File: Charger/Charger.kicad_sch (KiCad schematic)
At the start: 9 parts, among them J1 Bat_ballanser_conn, J2 Battery_conn, J3 Power_conn, J4 Screen_SPInCtrlnPwr_Conn, J5 User_Interface_Conn, J8 Temp_Sens_Conn

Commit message: PCB V1
do przerobienia jedynie numery elementów na wartości jedno i drugi w miare poukladane tylko podmienic i posprawdzać
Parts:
- J3: footprint Connector_AMASS:AMASS_XT60PW-F_1x02_P7.20mm_Horizontal -> Connector_AMASS:AMASS_XT60PW-M_1x02_P7.20mm_Horizontal
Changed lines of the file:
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@@
 			)
 		)
-		(property "Footprint" "Connector_AMASS:AMASS_XT60PW-F_1x02_P7.20mm_Horizontal"
+		(property "Footprint" "Connector_AMASS:AMASS_XT60PW-M_1x02_P7.20mm_Horizontal"
 			(at 25.4 52.07 0)
 			(effects

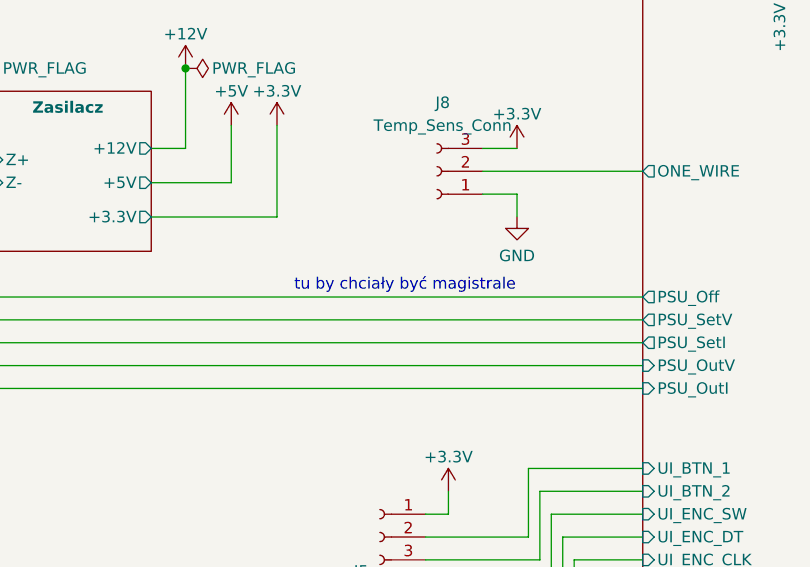
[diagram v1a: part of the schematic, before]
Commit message: Changed SPI connector and MUX pins
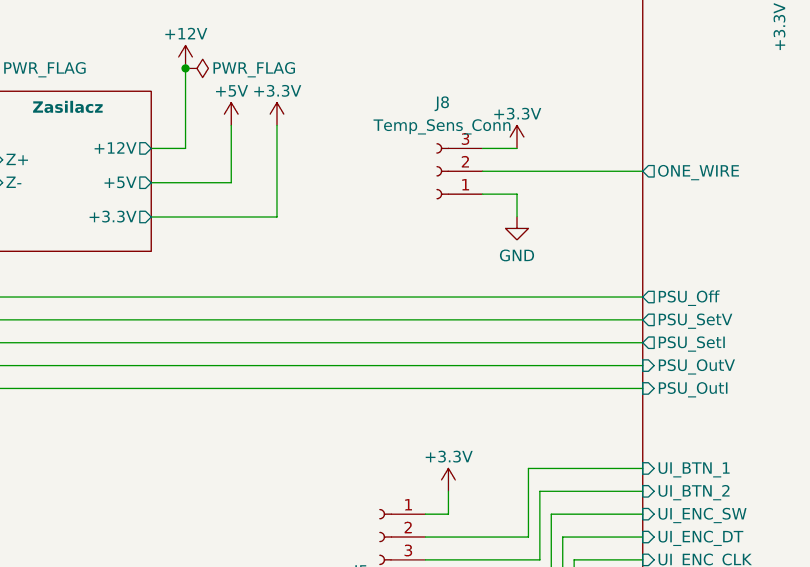
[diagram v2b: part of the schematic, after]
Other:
- note removed: "tu by chciały być magistrale"
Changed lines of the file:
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@@
-		)
-	)
-	(text "tu by chciały być magistrale"
-		(exclude_from_sim no)
-		(at 92.964 66.04 0)
-		(effects
-			(font
-				(size 1.27 1.27)
-			)
 		)
 	)

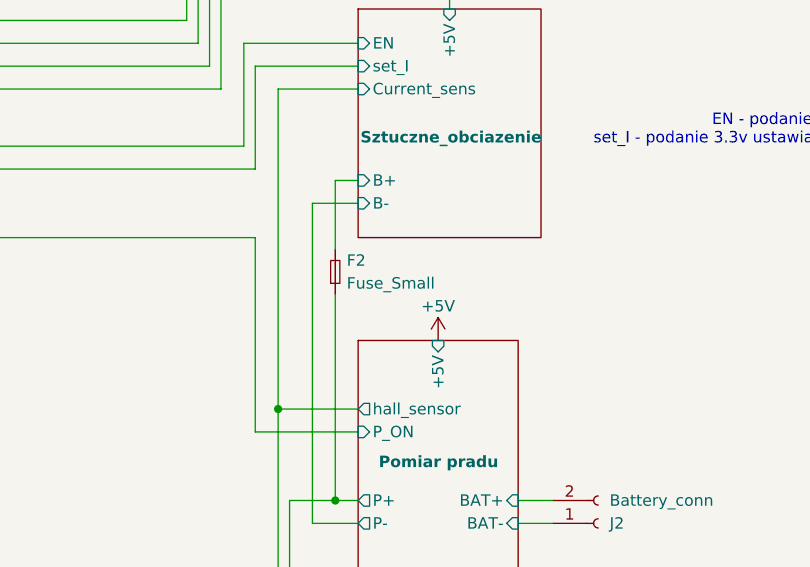
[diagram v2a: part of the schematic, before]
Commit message: up
zmienione kilka sciezek, dodane przelotki do masy i rezystor do adc
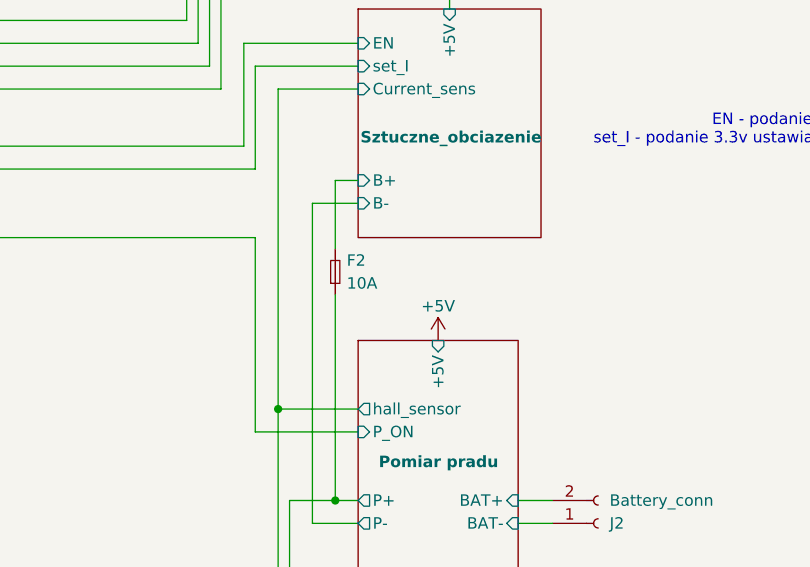
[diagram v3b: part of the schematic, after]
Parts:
- F2: value Fuse_Small -> 10A
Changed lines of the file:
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@@
 			)
 		)
-		(property "Value" "Fuse_Small"
+		(property "Value" "10A"
 			(at 213.36 107.9499 90)
 			(effects

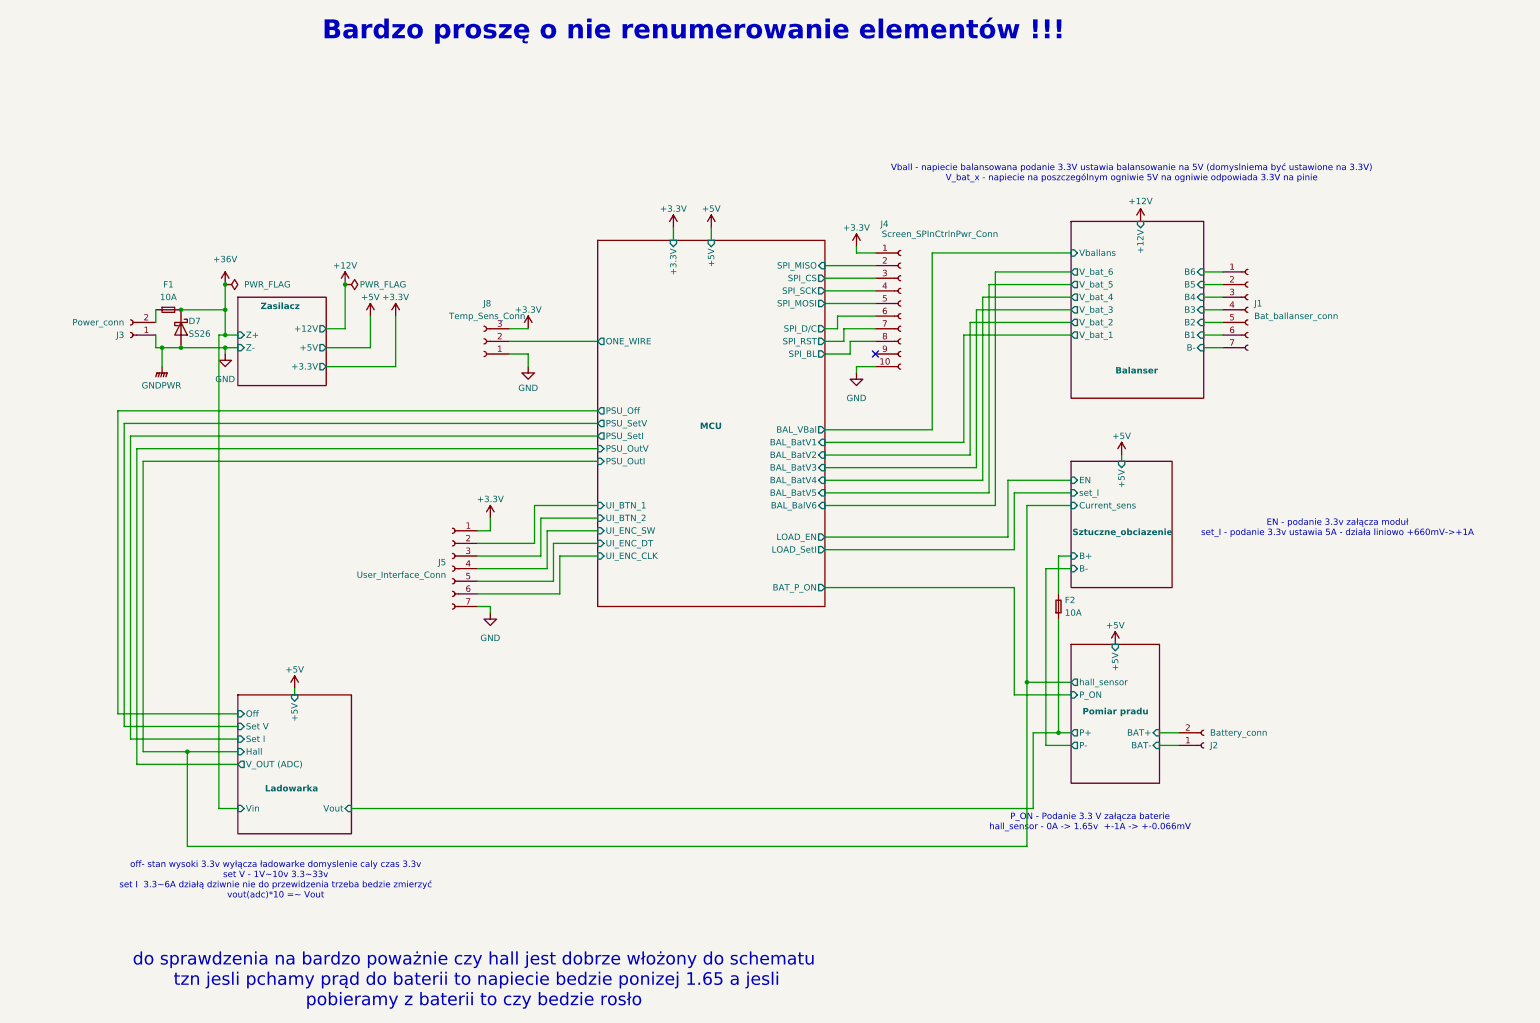
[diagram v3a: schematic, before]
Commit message: aktualizacja schematu
nie zmieniałem nic na pcb
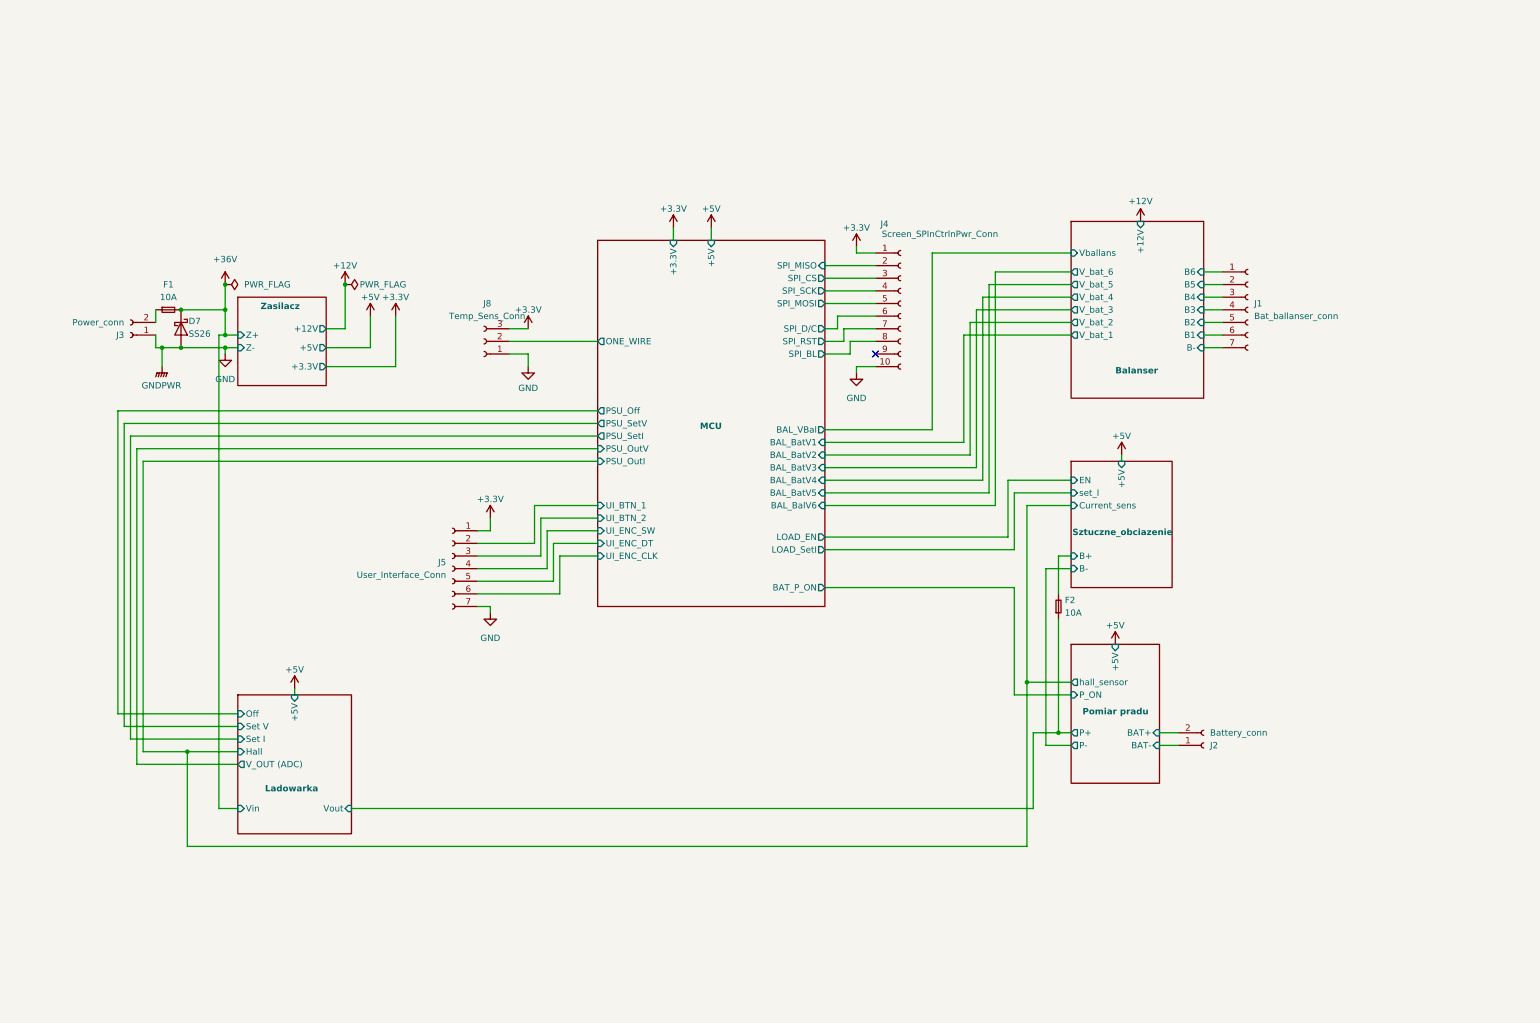
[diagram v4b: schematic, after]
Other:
- note removed: "Bardzo proszę o nie renumerowanie elementów !!!"
- note removed: "EN - podanie 3.3v załącza moduł set_I - podanie 3.3v ustawia 5A - działa liniowo +660mV->+1A"
- note removed: "P_ON - Podanie 3.3 V załącza baterie hall_sensor - 0A -> 1.65v +-1A -> +-0.066mV"
- note removed: "Vball - napiecie balansowana podanie 3.3V ustawia balansowanie na 5V (domyslniema być ustawione na 3.3V) V_bat_x - napiecie na poszczególnym ogniwie 5V na ogniwie odpowiada 3.3V na pinie"
- note removed: "do sprawdzenia na bardzo poważnie czy hall jest dobrze włożony do schematu tzn jesli pchamy prąd do baterii to napiecie bedzie ponizej 1.65 a jesli pobieramy z baterii to czy bedzie rosło"
- note removed: "off- stan wysoki 3.3v wyłącza ładowarke domyslenie caly czas 3.3v set V - 1V~10v 3.3~33v set I 3.3~6A działą dziwnie nie do przewidzenia trzeba bedzie zmierzyć vout(adc)*10 =~ Vout"
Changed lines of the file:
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@@
-		)
-	)
-	(text "EN - podanie 3.3v załącza moduł\nset_I - podanie 3.3v ustawia 5A - działa liniowo +660mV->+1A"
-		(exclude_from_sim no)
-		(at 268.224 90.932 0)
-		(effects
-			(font
-				(size 1.27 1.27)
-			)
-		)
-	)
-	(text "off- stan wysoki 3.3v wyłącza ładowarke domyslenie caly czas 3.3v\nset V - 1V~10v 3.3~33v\nset I  3.3~6A działą dziwnie nie do przewidzenia trzeba bedzie zmierzyć\nvout(adc)*10 =~ Vout"
-		(exclude_from_sim no)
-		(at 54.61 161.798 0)
-		(effects
-			(font
-				(size 1.27 1.27)
-			)
-		)
-	)
-	(text "Bardzo proszę o nie renumerowanie elementów !!!"
-		(exclude_from_sim no)
-		(at 138.684 -9.144 0)
-		(effects
-			(font
-				(size 3.81 3.81)
-				(thickness 0.762)
-				(bold yes)
-			)
-		)
-	)
-	(text "Vball - napiecie balansowana podanie 3.3V ustawia balansowanie na 5V (domyslniema być ustawione na 3.3V)\nV_bat_x - napiecie na poszczególnym ogniwie 5V na ogniwie odpowiada 3.3V na pinie \n"
-		(exclude_from_sim no)
-		(at 226.822 19.558 0)
-		(effects
-			(font
-				(size 1.27 1.27)
-			)
-		)
-	)
-	(text "do sprawdzenia na bardzo poważnie czy hall jest dobrze włożony do schematu\n tzn jesli pchamy prąd do baterii to napiecie bedzie ponizej 1.65 a jesli \npobieramy z baterii to czy bedzie rosło"
-		(exclude_from_sim no)
-		(at 94.488 181.864 0)
-		(effects
-			(font
-				(size 2.54 2.54)
-			)
-		)
-	)
-	(text "P_ON - Podanie 3.3 V załącza baterie\nhall_sensor - 0A -> 1.65v  +-1A -> +-0.066mV"
-		(exclude_from_sim no)
-		(at 218.44 150.114 0)
-		(effects
-			(font
-				(size 1.27 1.27)
-			)
 		)
 	)
